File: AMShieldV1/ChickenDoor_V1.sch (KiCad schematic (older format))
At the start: 38 parts

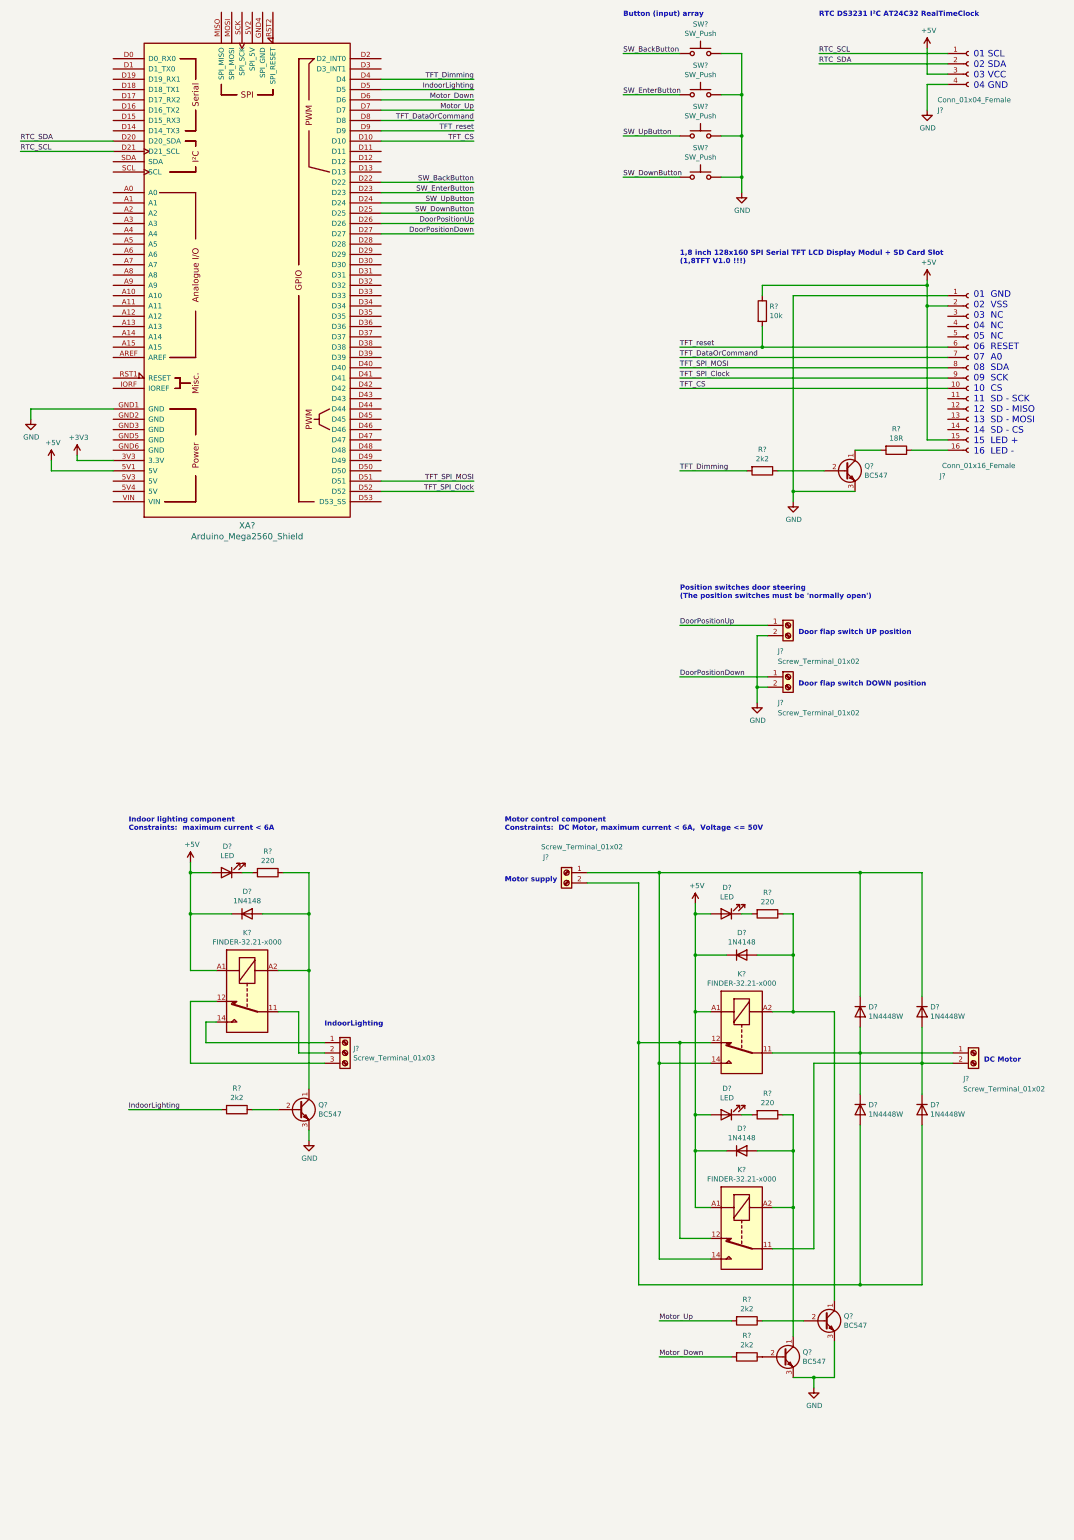
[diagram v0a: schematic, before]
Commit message: Built up the stripboard solution. Minor changes in the circuit. Updated the readme.
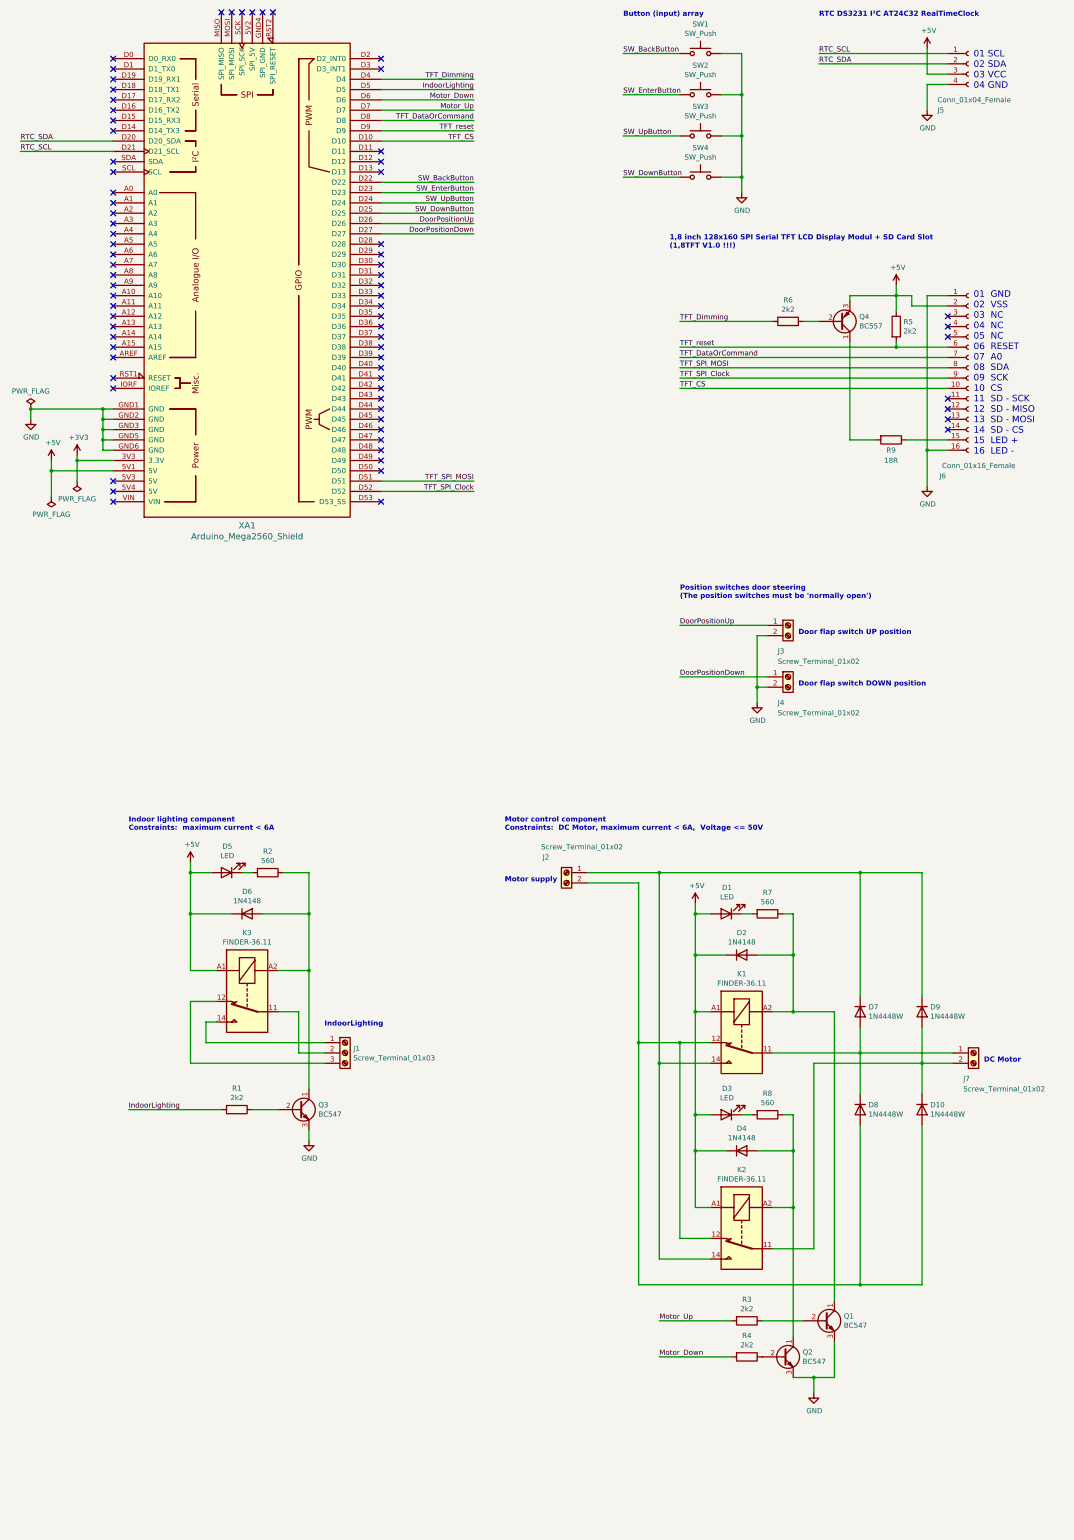
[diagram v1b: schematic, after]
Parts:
- removed K? (x3): FINDER-32.21-x000, Relay_THT:Relay_SPST_Finder_32.21-x300, symbol Relay:FINDER-32.21-x000
- removed Q?: BC547, Package_TO_SOT_THT:TO-92_Inline, symbol Transistor_BJT:BC547
- added K1, K2, K3: FINDER-36.11, Relay_THT:Relay_SPDT_Finder_36.11, symbol Relay:FINDER-36.11
- added Q4: BC557, Package_TO_SOT_THT:TO-92_Inline, symbol Transistor_BJT:BC557
- D1, D3, D5: renamed from D?; footprint (none) -> LED_THT:LED_D5.0mm
- J1: renamed from J?; footprint (none) -> TerminalBlock_MetzConnect:TerminalBlock_MetzConnect_Type011_RT05503HBWC_1x03_P5.00mm_Horizontal
- J2, J3, J4, J7: renamed from J?; footprint (none) -> TerminalBlock_MetzConnect:TerminalBlock_MetzConnect_Type011_RT05502HBWC_1x02_P5.00mm_Horizontal
- R1, R3, R4, R6, R9: renamed from R?; footprint (none) -> Resistor_THT:R_Axial_DIN0207_L6.3mm_D2.5mm_P10.16mm_Horizontal
- R2, R7, R8: renamed from R?; value 220 -> 560; footprint (none) -> Resistor_THT:R_Axial_DIN0207_L6.3mm_D2.5mm_P10.16mm_Horizontal
- R5: renamed from R?; value 10k -> 2k2; footprint (none) -> Resistor_THT:R_Axial_DIN0207_L6.3mm_D2.5mm_P10.16mm_Horizontal
- SW1, SW2, SW3, SW4: renamed from SW?; footprint (none) -> Button_Switch_THT:SW_PUSH_6mm_H9.5mm
- XA1: renamed from XA?; footprint (none) -> arduino:Arduino_Mega2560_Shield
- gave numbers to parts that had none: 12
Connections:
- net +5V: now also K1.A1, K2.A1, K3.A1, Q4.3 (E); no longer J6.15 (Pin_15)
- net GND: now also J6.16 (Pin_16), XA1.GND2 (GND), XA1.GND3 (GND), XA1.GND5 (GND), XA1.GND6 (GND)
- net at R9.1: now also J6.15 (Pin_15); no longer J6.16 (Pin_16)
- net at R9.2: now also Q4.1 (C)
- net at R6.1: now also Q4.2 (B)
- net at D7.2 (A), D8.1 (K), J7.1 (Pin_1): now also K1.11
- net at D10.2 (A), D8.2 (A), J2.2 (Pin_2): now also K1.12, K2.12
- net at D7.1 (K), D9.1 (K), J2.1 (Pin_1): now also K1.14, K2.14
- net at D2.2 (A), Q1.1 (C), R7.1: now also K1.A2
- net at D10.1 (K), D9.2 (A), J7.2 (Pin_2): now also K2.11
- net at D4.2 (A), Q2.1 (C), R8.1: now also K2.A2
- net at J1.2 (Pin_2): now also K3.11
- net at J1.3 (Pin_3): now also K3.12
- net at J1.1 (Pin_1): now also K3.14
- net at D6.2 (A), Q3.1 (C), R2.1: now also K3.A2
- no-connect marks 0 -> 74
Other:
- moved on the sheet: R5, R6, R9

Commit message: First draft of the PCB with updated schematic.
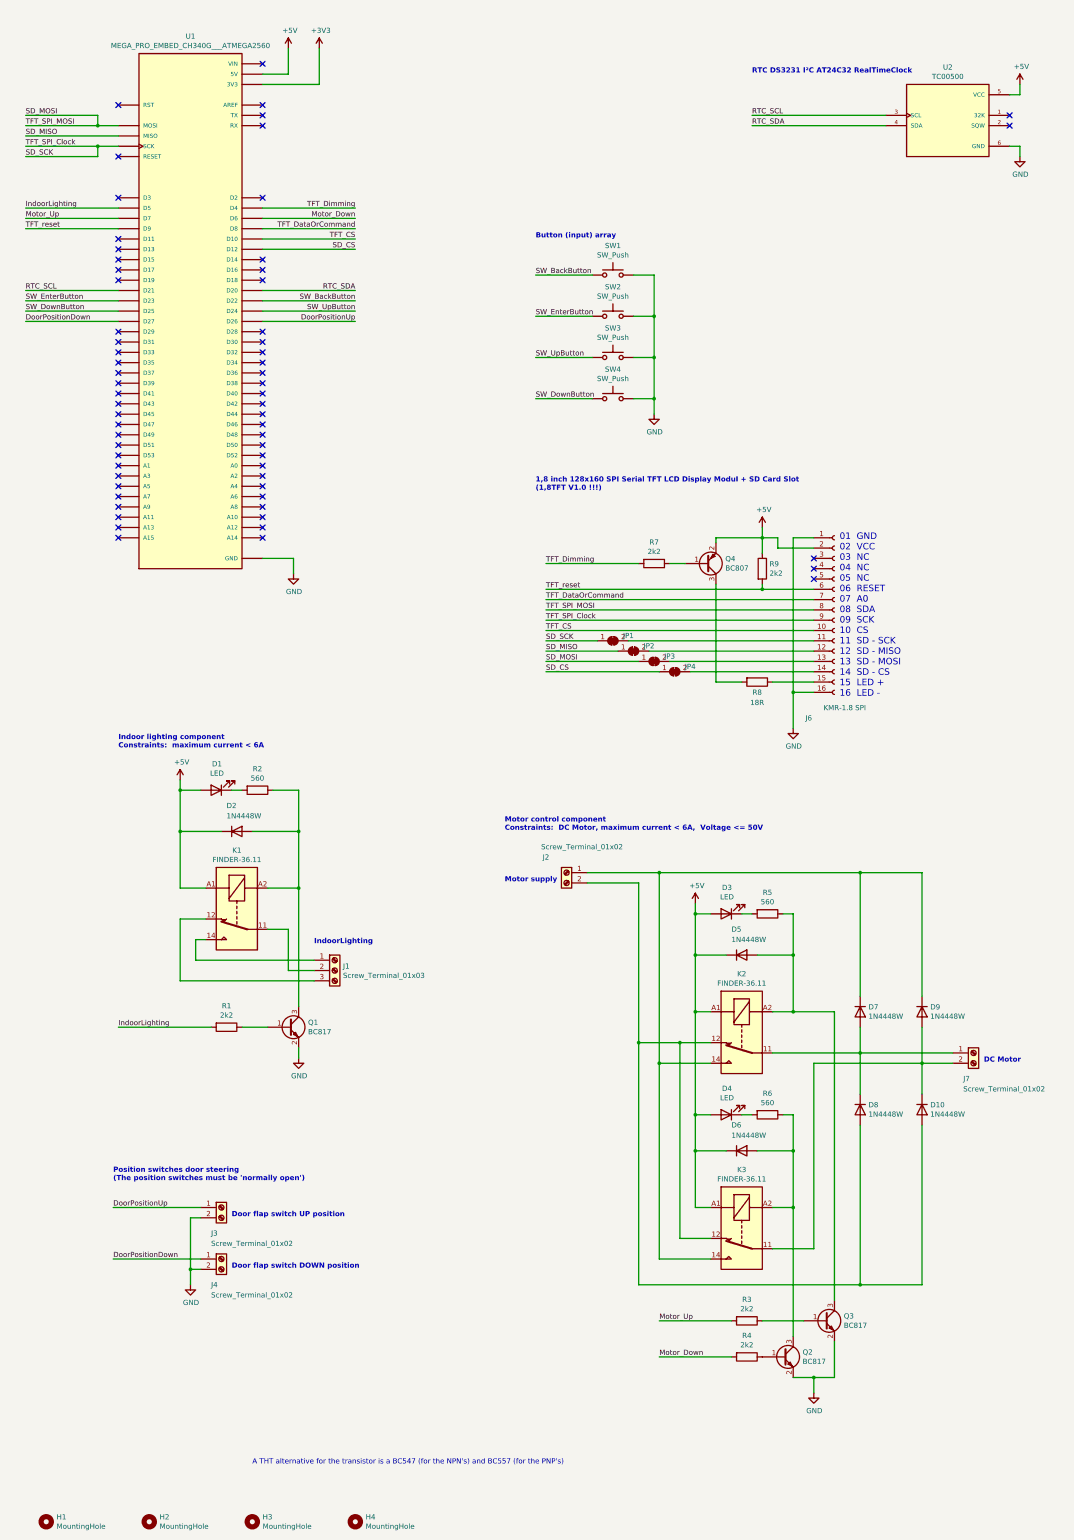
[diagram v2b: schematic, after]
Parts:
- removed D2, D4, D6: 1N4148, Diode_THT:D_DO-35_SOD27_P7.62mm_Horizontal, symbol Diode:1N4148
- removed J5: Conn_01x04_Female, symbol Connector:Conn_01x04_Female
- removed Q1, Q2, Q3: BC547, Package_TO_SOT_THT:TO-92_Inline, symbol Transistor_BJT:BC547
- removed Q4: BC557, Package_TO_SOT_THT:TO-92_Inline, symbol Transistor_BJT:BC557
- removed XA1: Arduino_Mega2560_Shield, arduino:Arduino_Mega2560_Shield, symbol arduino:Arduino_Mega2560_Shield
- added D2, D5, D6: 1N4448W, Diode_SMD:D_SOD-123, symbol Diode:1N4448W
- added H1, H2, H3, H4: MountingHole, MountingHole:MountingHole_4.3mm_M4_DIN965, symbol Mechanical:MountingHole
- added JP1, JP2, JP3, JP4: SolderJumper_2_Bridged, Jumper:SolderJumper-2_P1.3mm_Bridged_RoundedPad1.0x1.5mm, symbol Jumper:SolderJumper_2_Bridged
- added Q1, Q2, Q3: BC817, Package_TO_SOT_SMD:SOT-23, symbol Transistor_BJT:BC817
- added Q4: BC807, Package_TO_SOT_SMD:SOT-23, symbol Transistor_BJT:BC807
- added U1: MEGA_PRO_EMBED_CH340G___ATMEGA2560, MEGA_PRO_EMBED_CH340G___ATMEGA2560:MODULE_MEGA_PRO_EMBED_CH340G___ATMEGA2560, symbol MEGA_PRO_EMBED_CH340G___ATMEGA2560:MEGA_PRO_EMBED_CH340G___ATMEGA2560
- added U2: TC00500, TC00500_DS3231_AT24C32:MODULE_TC00500_FHk_BatteryUpside, symbol TC00500:TC00500
- D1: renamed from D5; footprint LED_THT:LED_D5.0mm -> LED_SMD:LED_1206_3216Metric
- D3: renamed from D1; footprint LED_THT:LED_D5.0mm -> LED_SMD:LED_1206_3216Metric
- D4: renamed from D3; footprint LED_THT:LED_D5.0mm -> LED_SMD:LED_1206_3216Metric
- J1: footprint TerminalBlock_MetzConnect:TerminalBlock_MetzConnect_Type011_RT05503HBWC_1x03_P5.00mm_Horizontal -> TerminalBlock_Phoenix:TerminalBlock_Phoenix_MKDS-1,5-3-5.08_1x03_P5.08mm_Horizontal
- J2, J3, J4, J7: footprint TerminalBlock_MetzConnect:TerminalBlock_MetzConnect_Type011_RT05502HBWC_1x02_P5.00mm_Horizontal -> TerminalBlock_Phoenix:TerminalBlock_Phoenix_MKDS-1,5-2-5.08_1x02_P5.08mm_Horizontal
- J6: value Conn_01x16_Female -> KMR-1.8 SPI; footprint (none) -> KMR-1:KMR-1.8-SPI
- R1, R2, R3, R4: footprint Resistor_THT:R_Axial_DIN0207_L6.3mm_D2.5mm_P10.16mm_Horizontal -> Resistor_SMD:R_0805_2012Metric
- R5: renamed from R7; footprint Resistor_THT:R_Axial_DIN0207_L6.3mm_D2.5mm_P10.16mm_Horizontal -> Resistor_SMD:R_0805_2012Metric
- R6: renamed from R8; footprint Resistor_THT:R_Axial_DIN0207_L6.3mm_D2.5mm_P10.16mm_Horizontal -> Resistor_SMD:R_0805_2012Metric
- R7: renamed from R6; footprint Resistor_THT:R_Axial_DIN0207_L6.3mm_D2.5mm_P10.16mm_Horizontal -> Resistor_SMD:R_0805_2012Metric
- R8: renamed from R9; footprint Resistor_THT:R_Axial_DIN0207_L6.3mm_D2.5mm_P10.16mm_Horizontal -> Resistor_SMD:R_0805_2012Metric
- R9: renamed from R5; footprint Resistor_THT:R_Axial_DIN0207_L6.3mm_D2.5mm_P10.16mm_Horizontal -> Resistor_SMD:R_0805_2012Metric
- renumbered K3 to K1, K1 to K2, K2 to K3
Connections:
- net +3V3: now also U1.3V3_1 (3V3), U1.3V3_2 (3V3)
- net +5V: now also D2.1 (K), D5.1 (K), D6.1 (K), Q4.2 (E), U1.5V_1 (5V), U1.5V_2 (5V), U1.5V_3 (5V), U2.5 (VCC)
- net DoorPositionDown: now also U1.D27
- net DoorPositionUp: now also U1.D26
- net GND: now also Q1.2 (E), Q2.2 (E), Q3.2 (E), U1.GND_1 (GND), U1.GND_2 (GND), U1.GND_3 (GND), U2.6 (GND)
- net IndoorLighting: now also U1.D5
- net Motor_Down: now also U1.D6
- net Motor_Up: now also U1.D7
- net RTC_SCL: now also U1.D21, U2.3 (SCL)
- net RTC_SDA: now also U1.D20, U2.4 (SDA)
- net SW_BackButton: now also U1.D22
- net SW_DownButton: now also U1.D25
- net SW_EnterButton: now also U1.D23
- net SW_UpButton: now also U1.D24
- net TFT_CS: now also U1.D10
- net TFT_DataOrCommand: now also U1.D8
- net TFT_Dimming: now also U1.D4
- net TFT_reset: now also U1.D9
- net at J6.11 (Pin_11): now also JP1.2 (B)
- net at J6.12 (Pin_12): now also JP2.2 (B)
- net at J6.13 (Pin_13): now also JP3.2 (B)
- net at J6.14 (Pin_14): now also JP4.2 (B)
- net at R8.2: now also Q4.3 (C)
- net at K2.A2, R5.1: now also D5.2 (A), Q3.3 (C)
- net at K3.A2, R6.1: now also D6.2 (A), Q2.3 (C)
- net at R7.1: now also Q4.1 (B)
- net at R4.1: now also Q2.1 (B)
- net at R3.1: now also Q3.1 (B)
- net at K1.A2, R2.1: now also D2.2 (A), Q1.3 (C)
- net at R1.1: now also Q1.1 (B)
- net TFT_SPI_Clock renamed SD_SCK
- net SD_SCK: now also JP1.1 (A), U1.SCK
- net TFT_SPI_MOSI renamed SD_MOSI
- net SD_MOSI: now also JP3.1 (A), U1.MOSI
- new net: U1.VIN_1 (VIN), U1.VIN_2 (VIN)
- new net SD_CS: JP4.1 (A), U1.D12
- new net SD_MISO: JP2.1 (A), U1.MISO
- no-connect marks 74 -> 63
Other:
- note added: "01 GND\n02 VCC\n03 NC\n04 NC\n05 NC\n06 RESET\n07 A0\n08 SDA\n09 SCK\n10 CS\n11 SD - SCK\n12 SD - MISO\n13 SD - MOSI\n14 SD - CS\n15 LED +\n16 LED -"
- note added: "A THT alternative for the transistor is a BC547 (for the NPN's) and BC557 (for the PNP's)"
- note removed: "01 GND\n02 VSS\n03 NC\n04 NC\n05 NC\n06 RESET\n07 A0\n08 SDA\n09 SCK\n10 CS\n11 SD - SCK\n12 SD - MISO\n13 SD - MOSI\n14 SD - CS\n15 LED +\n16 LED -"
- note removed: "01 SCL\n02 SDA\n03 VCC\n04 GND"
- moved on the sheet: D1, J1, J3, J4, J6, K1, R1, R2, R7, R8, R9, SW1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
